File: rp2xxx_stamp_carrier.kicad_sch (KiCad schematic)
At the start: 30 parts, among them J10 Conn_01x10, J11 microSD, J12 Conn_01x08, J14 Conn_01x08, J15 Conn_01x08, J16 Conn_01x08, J2 Conn_Pi_SWD, J2 Conn_Pi_UART, J2 Conn_Stemma_QT, J3 Conn_SPI, J6 DVI-D_Mini, J8 Conn_PMOD, J9 Conn_01x08, SW1 BTN_RESET, SW2 BTN_BOOTSEL, SW4 BTN_USR1, SW5 BTN_USR2, U3 rp2xxx_Stamp_XL

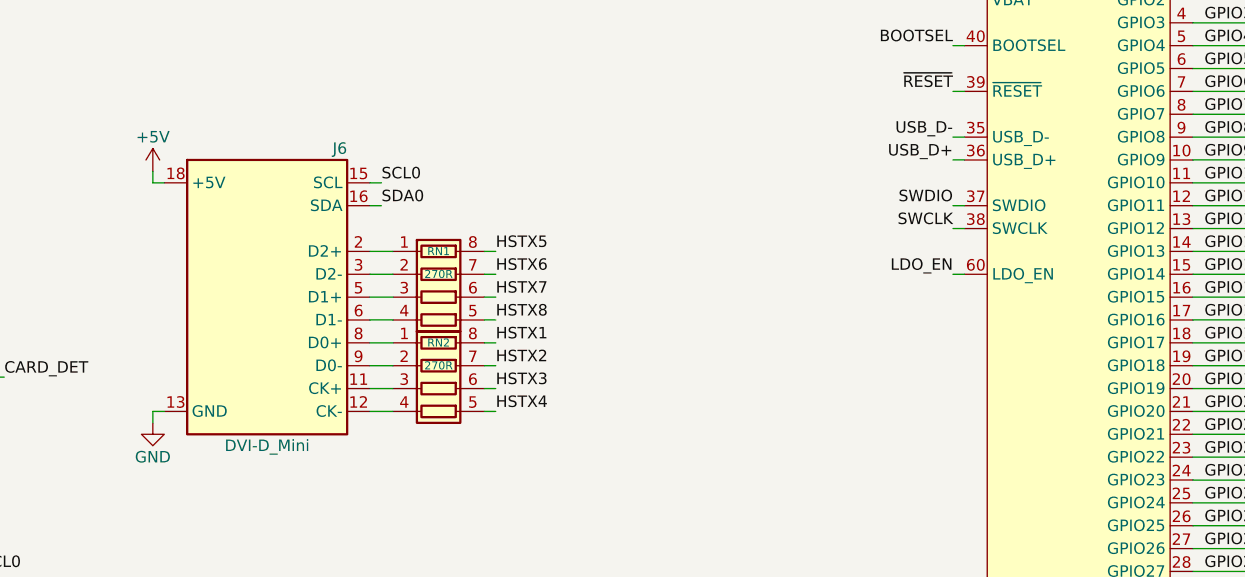
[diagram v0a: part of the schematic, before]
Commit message: Rev 2
Fixed HDMI connector
Swapped RST and BOOTSEL buttons to match Stamp
Added BAT_STAT to Stamp
Changed 2x silk back to single line
Adjusted Name silkscreen
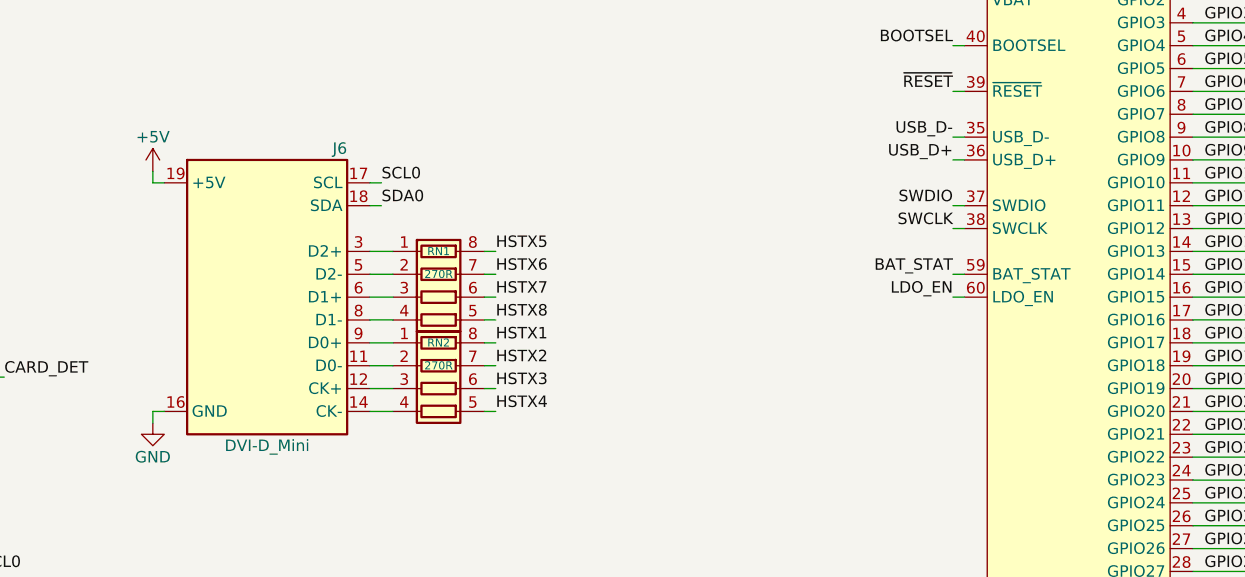
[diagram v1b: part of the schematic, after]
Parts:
- U3: symbol RP2040_Stamp:rp2xxx_Stamp_XL -> RP2040_Stamp:RP2350_Stamp_XL
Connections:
- net +5V: now also J6.19 (+5V); no longer J6.18 (+5V)
- net GND: now also J6.16 (GND); no longer J6.1 (D2S)
- net GPIO4: now also J6.18 (SDA); no longer J6.16 (SDA)
- net GPIO5: now also J6.17 (SCL); no longer J6.15 (SCL)
- net at RN2.1 (R1.1): now also J6.9 (D0+); no longer J6.8 (D0+)
- net at RN2.2 (R2.1): now also J6.11 (D0-); no longer J6.9 (D0-)
- net at RN2.3 (R3.1): now also J6.12 (CK+); no longer J6.11 (CK+)
- net at RN2.4 (R4.1): now also J6.14 (CK-); no longer J6.12 (CK-)
- net at RN1.1 (R1.1): now also J6.3 (D2+); no longer J6.2 (D2+)
- net at RN1.2 (R2.1): now also J6.5 (D2-); no longer J6.3 (D2-)
- net at RN1.3 (R3.1): now also J6.6 (D1+); no longer J6.5 (D1+)
- net at RN1.4 (R4.1): now also J6.8 (D1-); no longer J6.6 (D1-)
- net BAT_STAT: now reaches U3.59 (BAT_STAT)
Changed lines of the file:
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@@
 	(wire
 		(pts
+			(xy 172.72 80.01) (xy 173.99 80.01)
+		)
+		(stroke
+			(width 0)
+			(type default)
+		)
+	)
+	(wire
+		(pts
 			(xy 128.27 163.83) (xy 128.27 167.64)
 		)
@@
 	)
 	(label "LDO_EN"
-		(at 172.72 77.47 180)
+		(at 172.72 80.01 180)
 		(fields_autoplaced yes)
 		(effects
@@
 		)
 	)
+	(label "BAT_STAT"
+		(at 172.72 77.47 180)
+		(fields_autoplaced yes)
+		(effects
+			(font
+				(size 1.27 1.27)
+			)
+			(justify right bottom)
+		)
+	)
 	(label "A0"
 		(at 195.58 153.67 180)
@@
 	)
 	(symbol
-		(lib_id "RP2040_Stamp:rp2xxx_Stamp_XL")
+		(lib_id "RP2040_Stamp:RP2350_Stamp_XL")
 		(at 243.84 76.2 0)
 		(unit 2)
@@
 	)
 	(symbol
-		(lib_id "RP2040_Stamp:rp2xxx_Stamp_XL")
+		(lib_id "RP2040_Stamp:RP2350_Stamp_XL")
 		(at 186.69 81.28 0)
 		(unit 1)
@@
 			)
 		)
-		(property "Datasheet" "http://pinoutguide.com/PortableDevices/mini_hdmi_pinout.shtml"
+		(property "Datasheet" "https://wmsc.lcsc.com/wmsc/upload/file/pdf/v2/lcsc/2210210000_XUNPU-HDMI-101S_C720620.pdf"
 			(at 95.504 97.282 0)
 			(effects

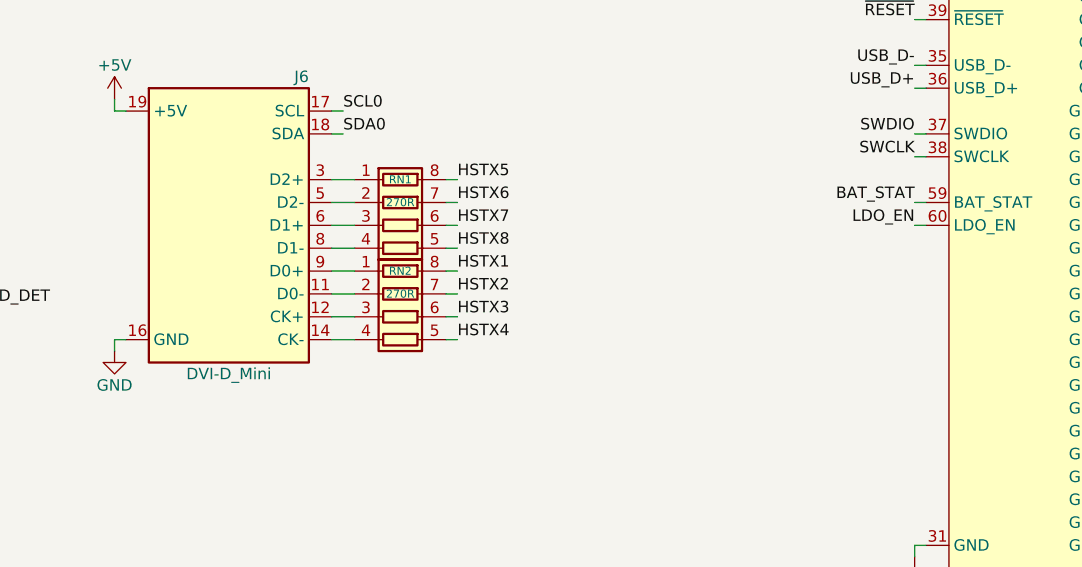
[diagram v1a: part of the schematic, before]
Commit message: Rev 3
- USB Switch jumper open by default
- Power USB Host from 5V not VBUS
- Fix SPI pin silkscreen
- Add test points for USB D+/D-
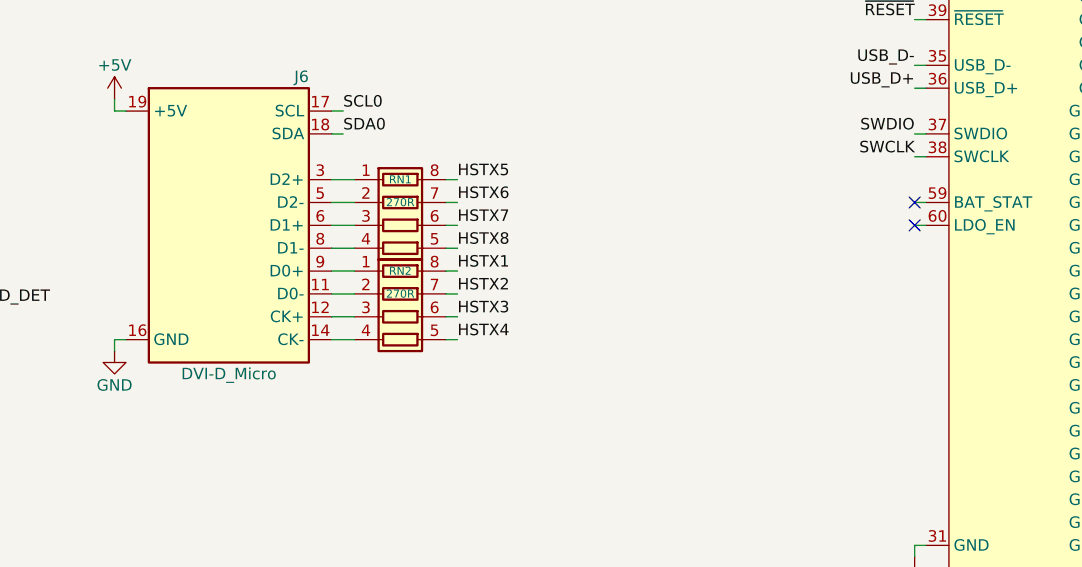
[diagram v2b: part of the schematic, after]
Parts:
- J6: value DVI-D_Mini -> DVI-D_Micro
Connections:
- net BAT_STAT: no longer names the net of U3.59 (BAT_STAT)
- net LDO_EN: no longer names the net of U3.60 (LDO_EN)
- no-connect marks 3 -> 5
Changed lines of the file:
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@@
 	)
 	(no_connect
+		(at 172.72 80.01)
+	)
+	(no_connect
+		(at 172.72 77.47)
+	)
+	(no_connect
 		(at 49.53 81.28)
 	)
@@
 		)
 	)
-	(label "LDO_EN"
-		(at 172.72 80.01 180)
-		(fields_autoplaced yes)
-		(effects
-			(font
-				(size 1.27 1.27)
-			)
-			(justify right bottom)
-		)
-	)
 	(label "GPIO23"
 		(at 200.66 100.33 0)
@@
 		)
 	)
-	(label "BAT_STAT"
-		(at 172.72 77.47 180)
-		(fields_autoplaced yes)
-		(effects
-			(font
-				(size 1.27 1.27)
-			)
-			(justify right bottom)
-		)
-	)
 	(label "A0"
 		(at 195.58 153.67 180)
@@
 			)
 		)
-		(property "Value" "DVI-D_Mini"
+		(property "Value" "DVI-D_Micro"
 			(at 96.52 96.52 0)
 			(effects

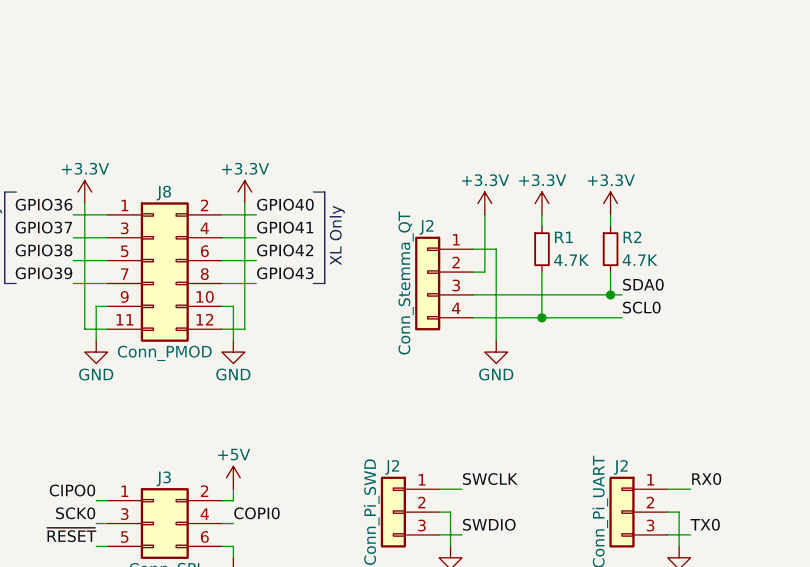
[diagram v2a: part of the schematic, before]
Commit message: Rev 3.1, add README, and LICENSE
- Fixed the microSD pin silkscreen
- Updated BOM
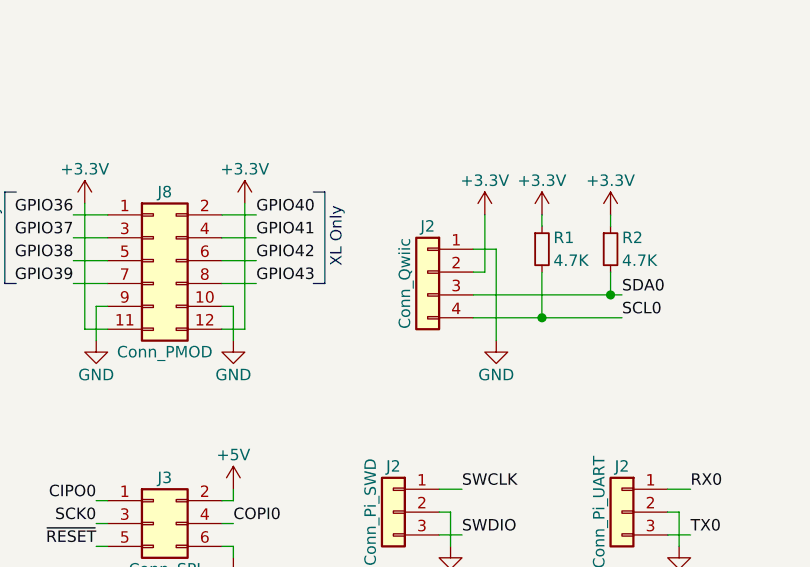
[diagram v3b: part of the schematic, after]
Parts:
- J10: LCSC (none) -> C2905418
- J12, J14, J15, J16, J9: LCSC (none) -> C27438
- J2: value Conn_Stemma_QT -> Conn_Qwiic
- J3: LCSC (none) -> C2685145
- J8: LCSC (none) -> C2911299
- JP10, JP11, JP12, JP13: now left out of the parts list
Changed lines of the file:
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@@
 			)
 		)
-		(property "Description" ""
+		(property "Description" "Red"
 			(at 102.87 35.56 0)
 			(effects
@@
 			)
 		)
-		(property "Value" "Conn_Stemma_QT"
+		(property "Value" "Conn_Qwiic"
 			(at 123.19 138.43 90)
 			(effects
@@
 		(unit 1)
 		(exclude_from_sim no)
-		(in_bom yes)
+		(in_bom no)
 		(on_board yes)
 		(dnp no)
@@
 			)
 		)
-		(property "Description" "Jumper, 3-pole, pins 1+2 closed/bridged"
+		(property "Description" ""
 			(at 236.22 153.67 0)
 			(effects
@@
 			)
 		)
-		(property "Description" "4 resistor network, parallel topology"
+		(property "Description" ""
 			(at 115.57 90.17 0)
 			(effects
@@
 		(unit 1)
 		(exclude_from_sim no)
-		(in_bom yes)
+		(in_bom no)
 		(on_board yes)
 		(dnp no)
@@
 			)
 		)
-		(property "Description" "Jumper, 3-pole, pins 1+2 closed/bridged"
+		(property "Description" ""
 			(at 254 153.67 0)
 			(effects
@@
 			)
 		)
-		(property "Description" "Generic connector, single row, 01x10, script generated (kicad-library-utils/schlib/autogen/connector/)"
+		(property "Description" "do not mount, place in bag with board"
+			(at 57.15 120.65 0)
+			(effects
+				(font
+					(size 1.27 1.27)
+				)
+				(hide yes)
+			)
+		)
+		(property "LCSC" "C2905418"
 			(at 57.15 120.65 0)
 			(effects
@@
 			)
 		)
-		(property "Description" "4 resistor network, parallel topology"
+		(property "Description" ""
 			(at 115.57 80.01 0)
 			(effects
@@
 			)
 		)
-		(property "Description" ""
+		(property "Description" "TS-3025-A-A-B"
 			(at 63.5 45.72 0)
 			(effects
@@
 			)
 		)
-		(property "Description" "Jumper, 2-pole, closed/bridged"
+		(property "Description" ""
 			(at 118.11 35.56 0)
 			(effects
@@
 			)
 		)
-		(property "Description" "Generic connector, single row, 01x08, script generated (kicad-library-utils/schlib/autogen/connector/)"
+		(property "Description" "do not mount, place in bag with board"
+			(at 57.15 146.05 0)
+			(effects
+				(font
+					(size 1.27 1.27)
+				)
+				(hide yes)
+			)
+		)
+		(property "LCSC" "C27438"
 			(at 57.15 146.05 0)
 			(effects
@@
 		(unit 1)
 		(exclude_from_sim no)
-		(in_bom yes)
+		(in_bom no)
 		(on_board yes)
 		(dnp no)
@@
 			)
 		)
-		(property "Description" "Jumper, 3-pole, pins 1+2 closed/bridged"
+		(property "Description" ""
 			(at 200.66 153.67 0)
 			(effects
@@
 			)
 		)
-		(property "Description" "Generic connector, single row, 01x08, script generated (kicad-library-utils/schlib/autogen/connector/)"
+		(property "Description" "do not mount, place in bag with board"
+			(at 39.37 118.11 0)
+			(effects
+				(font
+					(size 1.27 1.27)
+				)
+				(hide yes)
+			)
+		)
+		(property "LCSC" "C27438"
 			(at 39.37 118.11 0)
 			(effects
@@
 			)
 		)
-		(property "Description" ""
+		(property "Description" "do not mount, place in bag with board"
+			(at 95.25 165.1 0)
+			(effects
+				(font
+					(size 1.27 1.27)
+				)
+				(hide yes)
+			)
+		)
+		(property "LCSC" "C2685145"
 			(at 95.25 165.1 0)
 			(effects
@@
 			)
 		)
-		(property "Description" "Generic connector, double row, 02x18, odd/even pin numbering scheme (row 1 odd numbers, row 2 even numbers), script generated (kicad-library-utils/schlib/autogen/connector/)"
+		(property "Description" "do not mount, place in bag with board"
+			(at 95.25 135.89 0)
+			(effects
+				(font
+					(size 1.27 1.27)
+				)
+				(hide yes)
+			)
+		)
+		(property "LCSC" "C2911299"
 			(at 95.25 135.89 0)
 			(effects
@@
 			)
 		)
-		(property "Description" "Jumper, 2-pole, closed/bridged"
+		(property "Description" ""
 			(at 60.96 88.9 0)
 			(effects
@@
 			)
 		)
-		(property "Description" ""
+		(property "Description" "TS-3025-A-A-B"
 			(at 63.5 33.02 0)
 			(effects
@@
 			)
 		)
-		(property "Description" ""
+		(property "Description" "TS-3025-A-A-B"
 			(at 63.5 26.67 0)
 			(effects
@@
 			)
 		)
-		(property "Description" "Generic connector, single row, 01x08, script generated (kicad-library-utils/schlib/autogen/connector/)"
+		(property "Description" "do not mount, place in bag with board"
+			(at 57.15 168.91 0)
+			(effects
+				(font
+					(size 1.27 1.27)
+				)
+				(hide yes)
+			)
+		)
+		(property "LCSC" "C27438"
 			(at 57.15 168.91 0)
 			(effects
@@
 		(unit 1)
 		(exclude_from_sim no)
-		(in_bom yes)
+		(in_bom no)
 		(on_board yes)
 		(dnp no)
@@
 			)
 		)
-		(property "Description" "Jumper, 3-pole, pins 1+2 closed/bridged"
+		(property "Description" ""
 			(at 218.44 153.67 0)
 			(effects
@@
 			)
 		)
-		(property "Description" ""
+		(property "Description" "TS-3025-A-A-B"
 			(at 63.5 39.37 0)
 			(effects
@@
 			)
 		)
-		(property "Description" "Generic connector, single row, 01x08, script generated (kicad-library-utils/schlib/autogen/connector/)"
+		(property "Description" "do not mount, place in bag with board"
+			(at 39.37 140.97 0)
+			(effects
+				(font
+					(size 1.27 1.27)
+				)
+				(hide yes)
+			)
+		)
+		(property "LCSC" "C27438"
 			(at 39.37 140.97 0)
 			(effects
@@
 			)
 		)
-		(property "Description" "Generic connector, single row, 01x08, script generated (kicad-library-utils/schlib/autogen/connector/)"
+		(property "Description" "do not mount, place in bag with board"
+			(at 39.37 163.83 0)
+			(effects
+				(font
+					(size 1.27 1.27)
+				)
+				(hide yes)
+			)
+		)
+		(property "LCSC" "C27438"
 			(at 39.37 163.83 0)
 			(effects
@@
 			)
 		)
-		(property "Description" "HDMI 1.4+ type C connector"
+		(property "Description" ""
 			(at 95.504 99.568 0)
 			(effects
